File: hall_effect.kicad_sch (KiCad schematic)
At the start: 26 parts, among them J2 Conn_01x03_Pin, J8 Conn_01x03_Pin, U12 OPA196xDGK, U13 OPA196xDGK, U2 OPA196xDGK, U4 OPA196xDGK

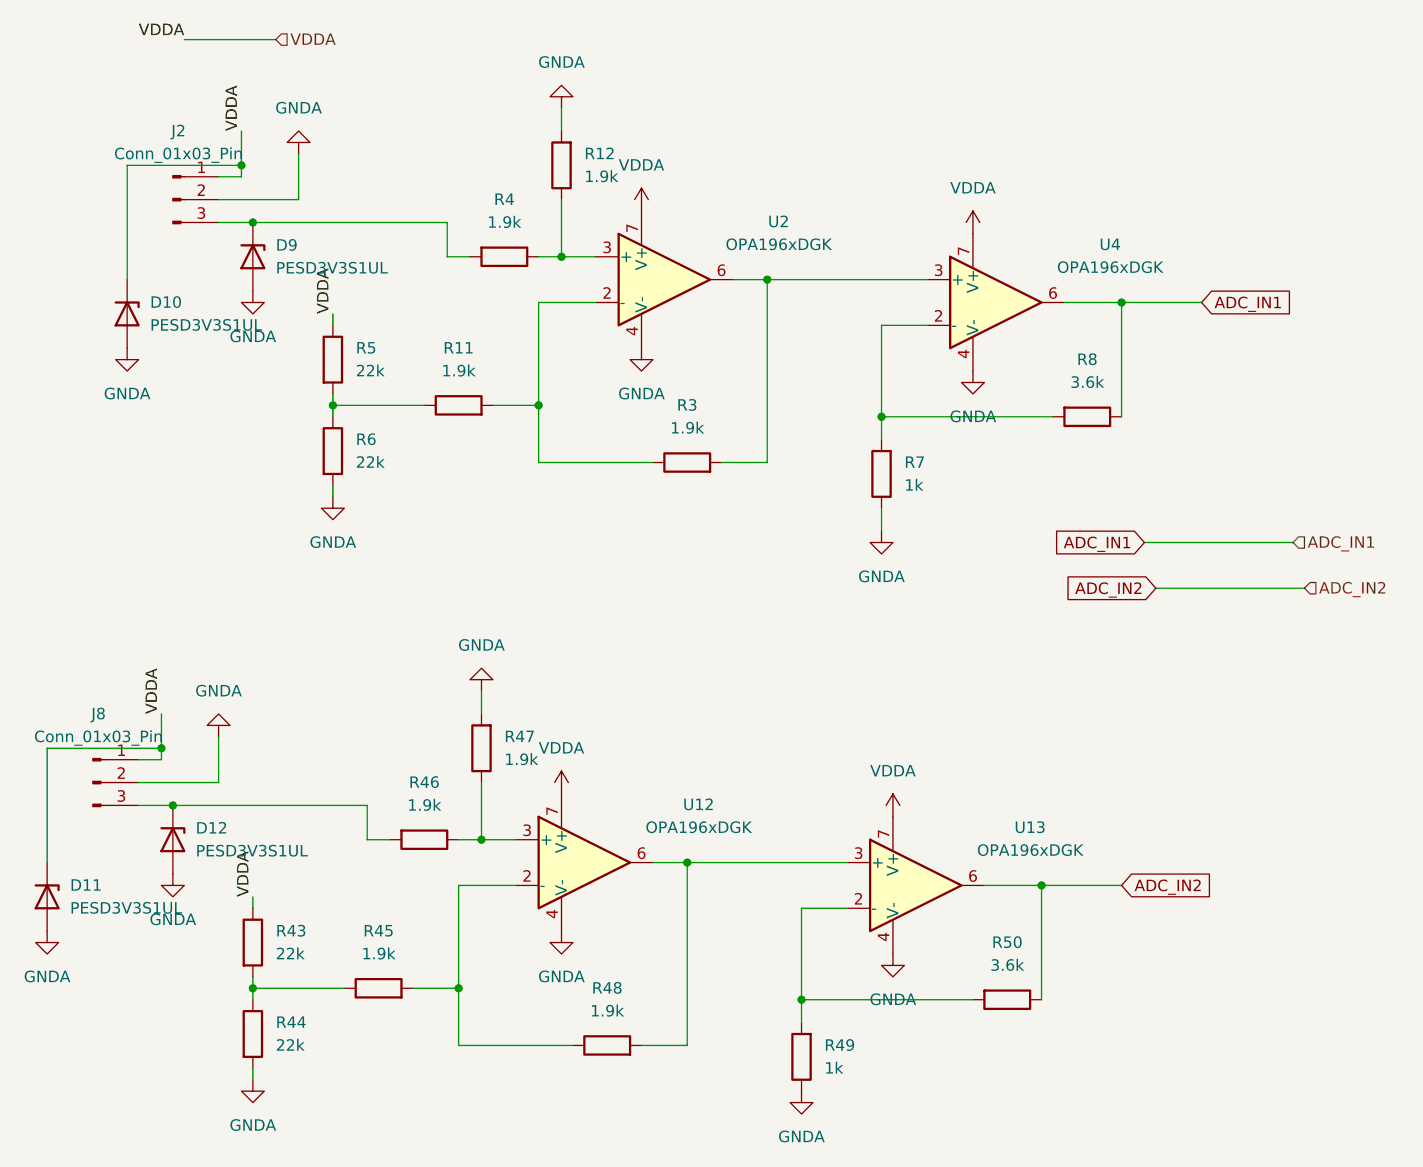
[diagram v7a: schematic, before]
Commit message: added 10 pin stlink and fixed a bunch of errors and warnings
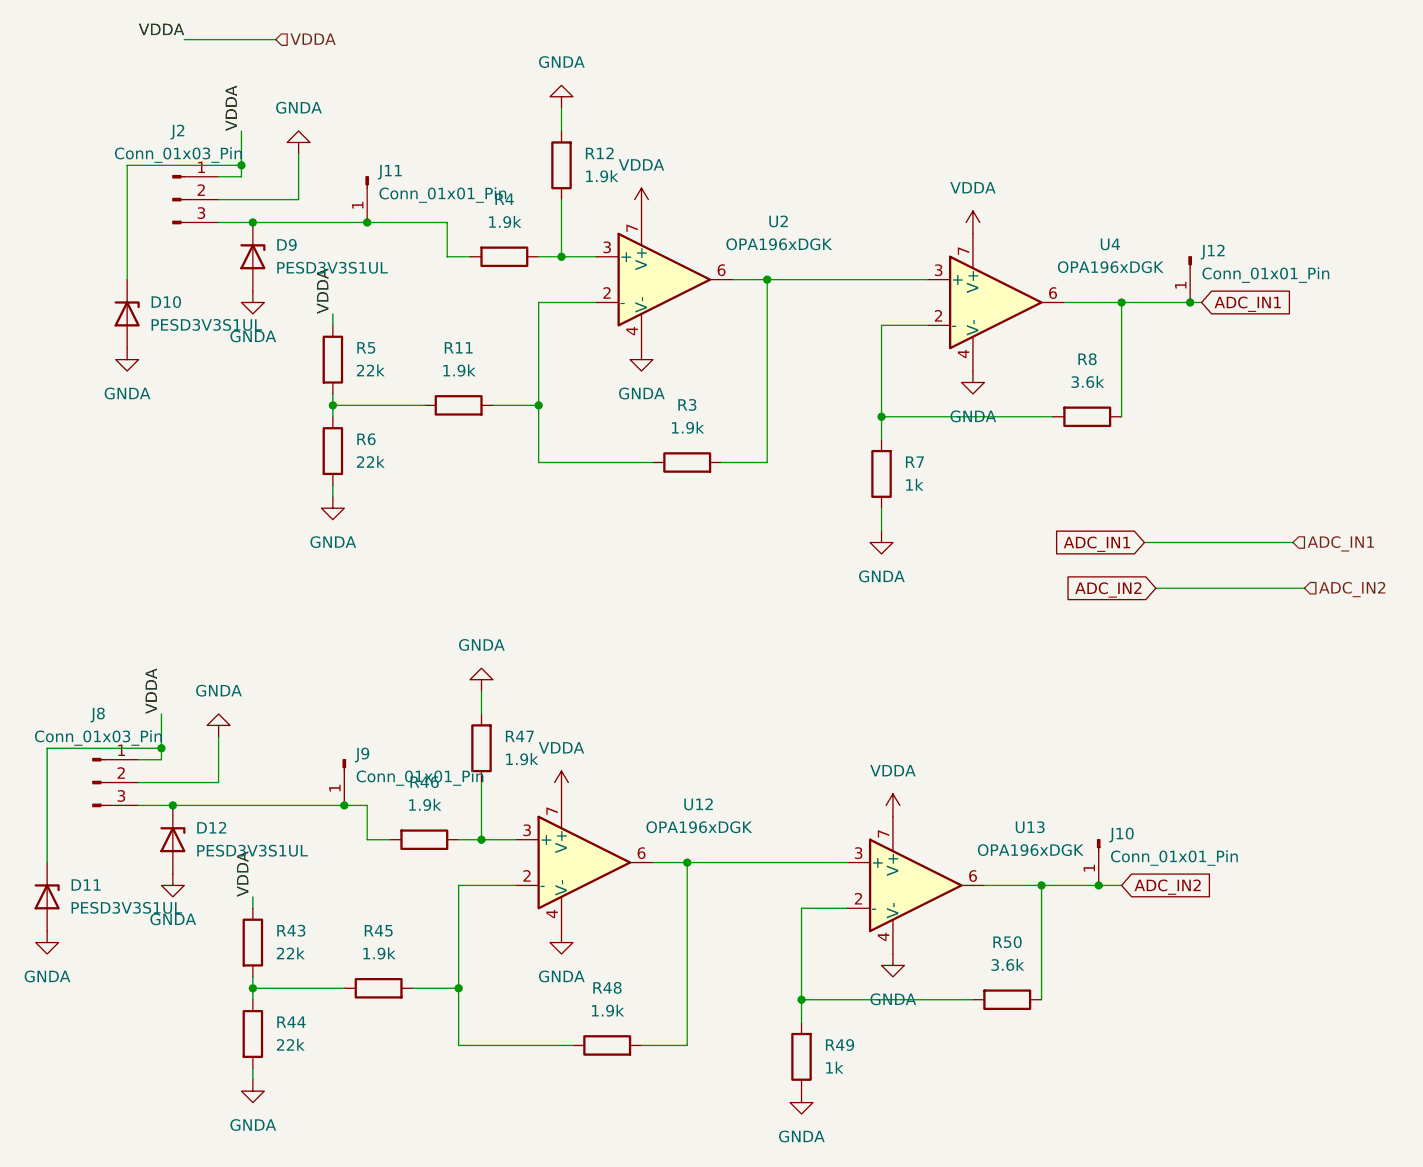
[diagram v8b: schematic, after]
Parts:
- added J10, J11, J12, J9: Conn_01x01_Pin, Connector_PinHeader_2.54mm:PinHeader_1x01_P2.54mm_Vertical, symbol Connector:Conn_01x01_Pin
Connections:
- net ADC_IN1: now also J12.1 (Pin_1)
- net ADC_IN2: now also J10.1 (Pin_1)
- net at D9.1 (K), J2.3 (Pin_3), R4.2: now also J11.1 (Pin_1)
- net at D12.1 (K), J8.3 (Pin_3), R46.2: now also J9.1 (Pin_1)
